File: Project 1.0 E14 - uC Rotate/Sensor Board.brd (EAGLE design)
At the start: 40 x 75 mm, 97 parts, among them IC1 LT1963EST-1.5, IC2 LT1963EST-1.5, IC4 LT1963EST-1.5

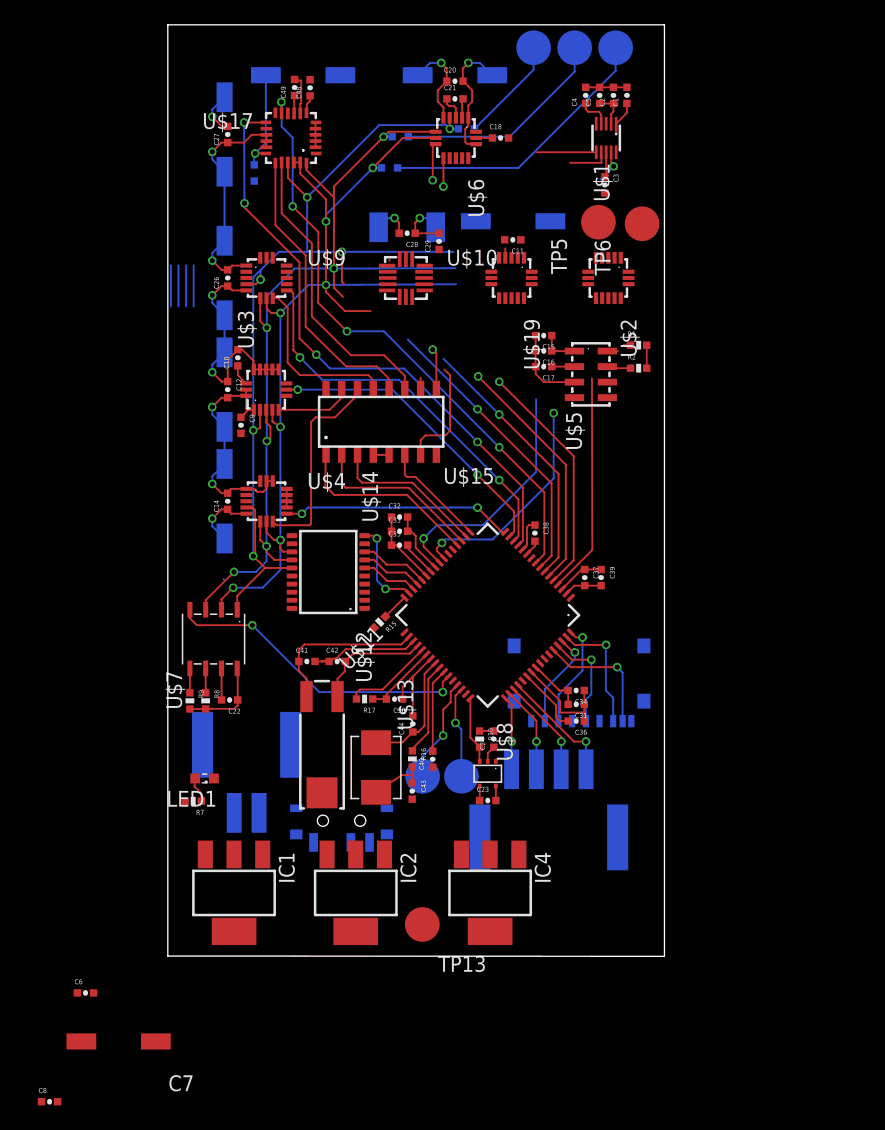
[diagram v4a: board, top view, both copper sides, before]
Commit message: Sensor Board: Chnaged 3:8 mux for a 4:10 mux and removed traces that were no longer valid, rerouting is now needed
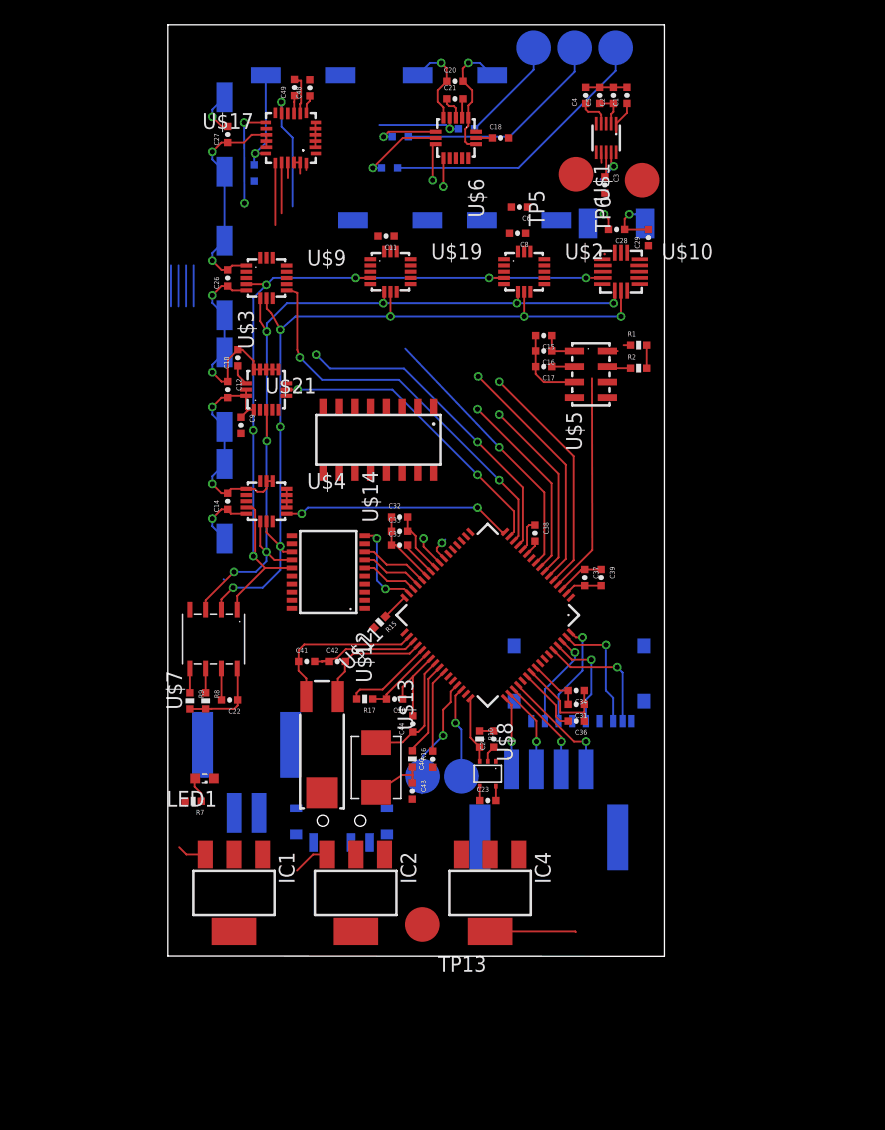
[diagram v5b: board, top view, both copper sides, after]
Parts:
- removed U$15: CD74HC138, Kas-Buffers & Level Shifters:SOIC-16
- added U$21: SN74HC42, Kas-Buffers & Level Shifters:SOIC-16
- moved C8 79.5 mm to (28.2, 58.2), turned to 180 degrees
- moved C7 73.6 mm to (28.3, 59.3), flipped to the bottom
- moved C6 72.3 mm to (28.3, 60.3), turned to 180 degrees
- moved U$10 17.3 mm to (36.5, 55.1)
- moved C29 16.9 mm to (38.7, 57.9)
- moved C19 16.9 mm to (36.1, 59.0)
- moved C28 16.9 mm to (36.1, 58.5)
- moved C11 10.2 mm to (17.6, 58.0)
- moved C54 9.91 mm to (17.9, 59.3)
- moved U$19 9.77 mm to (17.9, 55.1), turned to 0 degrees
- moved U$2 6.80 mm to (28.7, 55.1), turned to 0 degrees
- moved TP5 4.26 mm to (32.9, 63.0)
- moved TP6 3.51 mm to (38.2, 62.5)
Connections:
- removed net CS-ENABLE: U$11.P$17, U$15.P$6
- new net INT2-H3LIS331: U$11.P$10, U$2.P$9
- new net SPI-ADDR3: U$11.P$20, U$21.P$12
- net 3.3V: now also U$21.P$16; no longer U$15.P$16
- net CS-ADT7310: now also U$21.P$1; no longer U$11.P$43
- net CS-ADXL362: now also U$21.P$4; no longer U$15.P$10
- net CS-H3LIS331DLTR: no longer U$11.P$10
- net CS-LIS3DH: now also U$21.P$11; no longer U$15.P$13
- net CS-LPS331: now also U$21.P$10; no longer U$15.P$14
- net CS-LSGD: now also U$21.P$9; no longer U$15.P$15
- net CS-LSM303: now also U$21.P$3; no longer U$15.P$9
- net CS-LSM9D30-G: now also U$21.P$6; no longer U$15.P$12
- net CS-LSM9DS0-XM: now also U$21.P$5; no longer U$15.P$11
- net CS-MAX21000: now also U$21.P$2; no longer U$15.P$7
- net GND: now also U$21.P$8; no longer U$15.P$4, U$15.P$5, U$15.P$8
- net SPI-ADDR0: now also U$11.P$17, U$21.P$15; no longer U$11.P$20, U$15.P$1
- net SPI-ADDR1: now also U$11.P$18, U$21.P$14; no longer U$11.P$19, U$15.P$2
- net SPI-ADDR2: now also U$11.P$19, U$21.P$13; no longer U$11.P$18, U$15.P$3
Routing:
- net CS-ADT7310: track 25.0 -> 0.00 mm, vias 2 -> 0
- net SDA-0: track 26.3 -> 4.37 mm
- net CS-LSM9DS0-XM: track 23.9 -> 4.09 mm
- net SCL-0: track 22.9 -> 4.29 mm, vias 2 -> 1
- net CS-LSM9D30-G: track 23.5 -> 5.06 mm
- net LSM9D-INT-G: track 48.8 -> 31.8 mm, vias 4 -> 2
- net CS-LPS331: track 16.6 -> 0.00 mm
- net SPI-ADDR0: track 15.4 -> 0.00 mm
- net LSM9D-INT1-XM: track 48.7 -> 34.5 mm
- net CS-LIS3DH: track 14.2 -> 0.00 mm
- net SPI-ADDR1: track 13.9 -> 0.00 mm
- net SPI-ADDR2: track 12.5 -> 0.00 mm
- net CS-MAX21000: track 9.00 -> 0.00 mm
- net CS-ENABLE: track 8.79 -> 0.00 mm
- net SCLK-B: track 82.9 -> 74.8 mm, vias 6 -> 7
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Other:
- board text removed: "Change for 16:1 Mux"

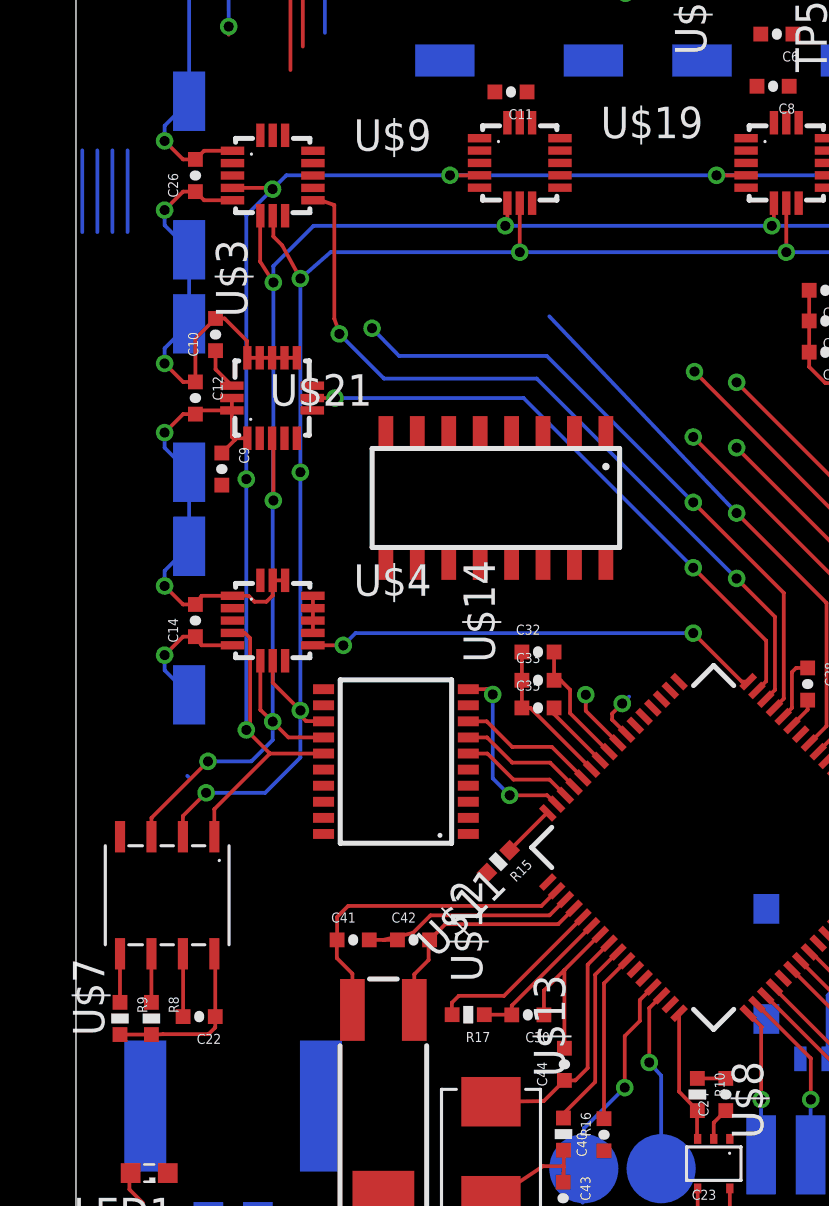
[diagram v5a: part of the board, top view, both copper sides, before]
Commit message: Sensor Test Board: Changed tmperature sensor for ADT7301 using a smaller package (SOT32-6). Reconnected CS traces in a organised fasion. Hid Power and GND traces.
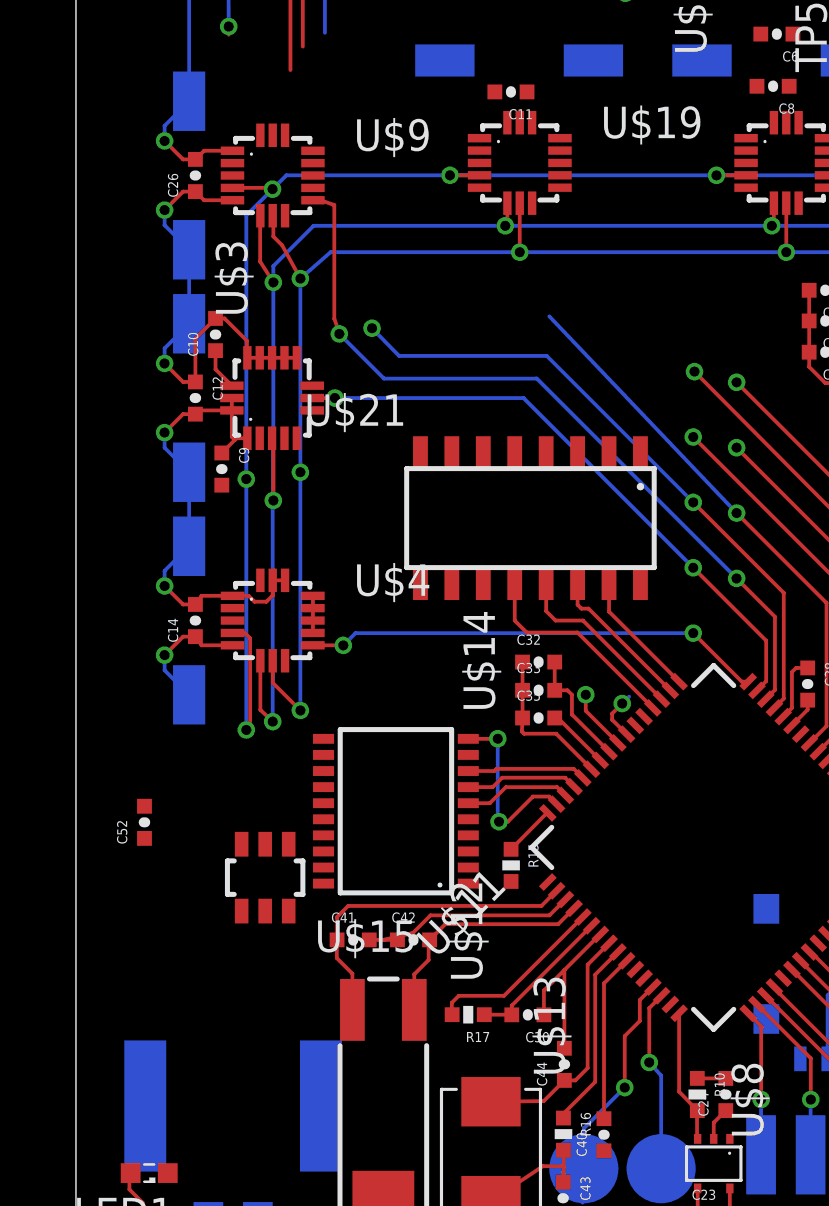
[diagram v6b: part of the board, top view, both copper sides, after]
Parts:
- removed C22: 0.1uF, Kas-Passives:0402-CAP
- removed R8, R9: 10k, Kas-Passives:0402-RES
- removed U$7: ADT7310, Kas-Sensors:SOIC-8(5X6.2)
- added C52: 0.1uF, Kas-Passives:0402-CAP
- added U$15: ADT7301, Kas-Sensors:SOT23-6
- moved U$14 2.01 mm to (12.9, 28.9)
- moved U$21 1.62 mm to (18.4, 40.8)
- moved R15 0.54 mm to (17.6, 26.7), turned to 270 degrees
- moved C35 0.41 mm to (18.7, 32.7)
- moved C32 0.41 mm to (18.7, 35.0)
- moved C33 0.41 mm to (18.7, 33.8)
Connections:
- net CS-LSGD renamed CS-LS3GD20
- removed net CS-ADT7310: U$21.P$1, U$7.P$4
- removed net CT-ADT7310: R8.1, U$7.P$6
- removed net INT-ADT7310: R9.1, U$7.P$5
- new net CS-ADT7301: U$15.P$5, U$21.P$11
- new net N$2: C52.1, U$15.P$3
- net 3.3V: no longer C22.1, R8.2, R9.2, U$7.P$8
- net CS-ADXL362: now also U$21.P$1; no longer U$21.P$4
- net CS-H3LIS331DLTR: now also U$21.P$2
- net CS-LIS3DH: now also U$21.P$7; no longer U$21.P$11
- net CS-MAX21000: now also U$21.P$4; no longer U$21.P$2
- net GND: now also C52.2, U$15.P$1; no longer C22.2, U$7.P$7
- net MISO-B: now also U$15.P$6; no longer U$7.P$2
- net MOSI-B: now also U$15.P$2; no longer U$7.P$3
- net SCLK-B: now also U$15.P$4; no longer U$7.P$1
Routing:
- net N$29: track 16.5 -> 0.00 mm
- net MOSI-B: track 73.7 -> 63.7 mm, vias 8 -> 7
- net MISO-B: track 74.5 -> 65.0 mm, vias 8 -> 7
- net SPI-ADDR3: track 0.00 -> 8.51 mm
- net SCLK-B: track 74.8 -> 67.0 mm
- net 3.3V: track 97.8 -> 90.5 mm
- net SPI-ADDR2: track 0.00 -> 7.22 mm
- net SPI-ADDR1: track 0.00 -> 6.01 mm
- net SPI-ADDR0: track 0.00 -> 5.11 mm
- net N$28: track 3.30 -> 0.00 mm
- net N$26: track 3.30 -> 0.00 mm
- net GND: track 91.7 -> 89.3 mm
- net INT-ADT7310: track 1.96 -> 0.00 mm
- net CT-ADT7310: track 1.96 -> 0.00 mm
- net MISO-A: track 5.57 -> 4.81 mm
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
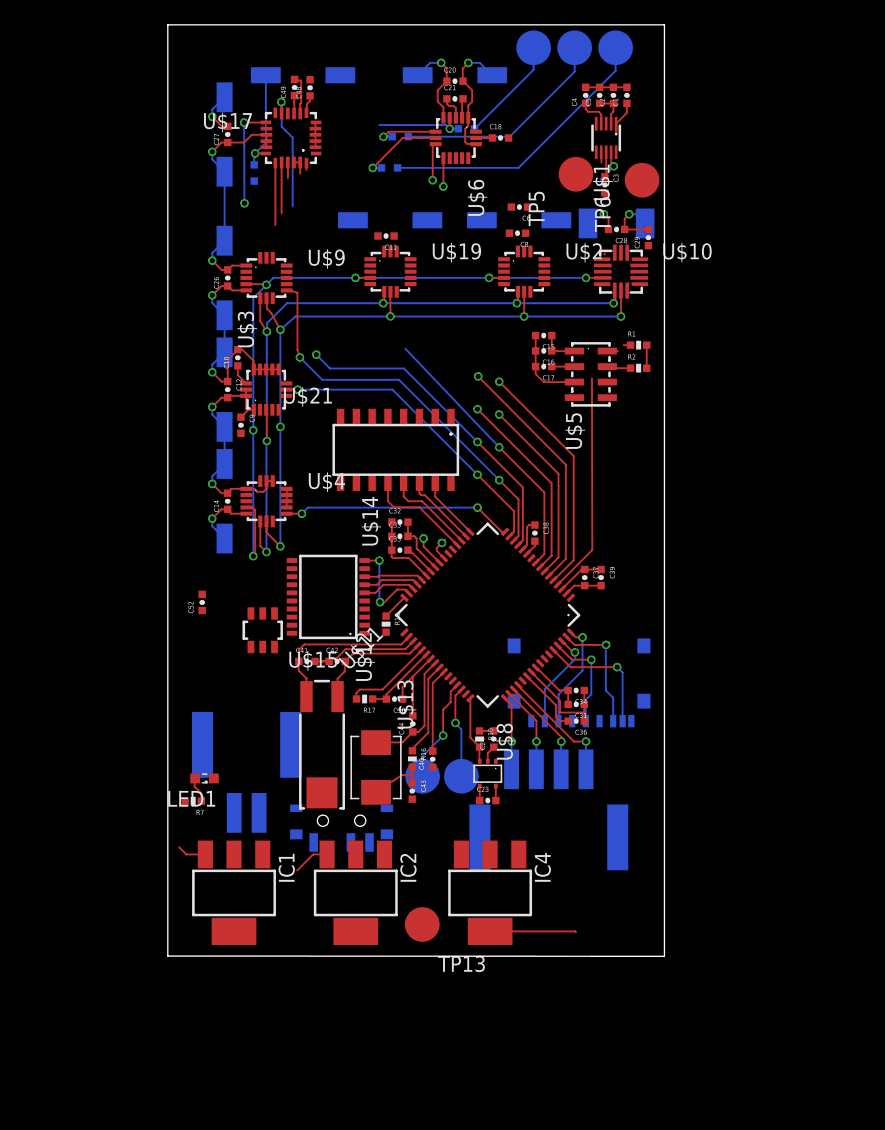
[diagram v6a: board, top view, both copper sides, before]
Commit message: Sensor Test Board: Swapped order of magnotometers, reorganised CS traces to prevent overlaps and connected new teperature sensor. Removed LS9D Vio bulk and decoupling capacitors. SPI test points were disconected but not removed. SPI vertical traces were spaced correctly with a minimum of 6x trace with spacing between traces.
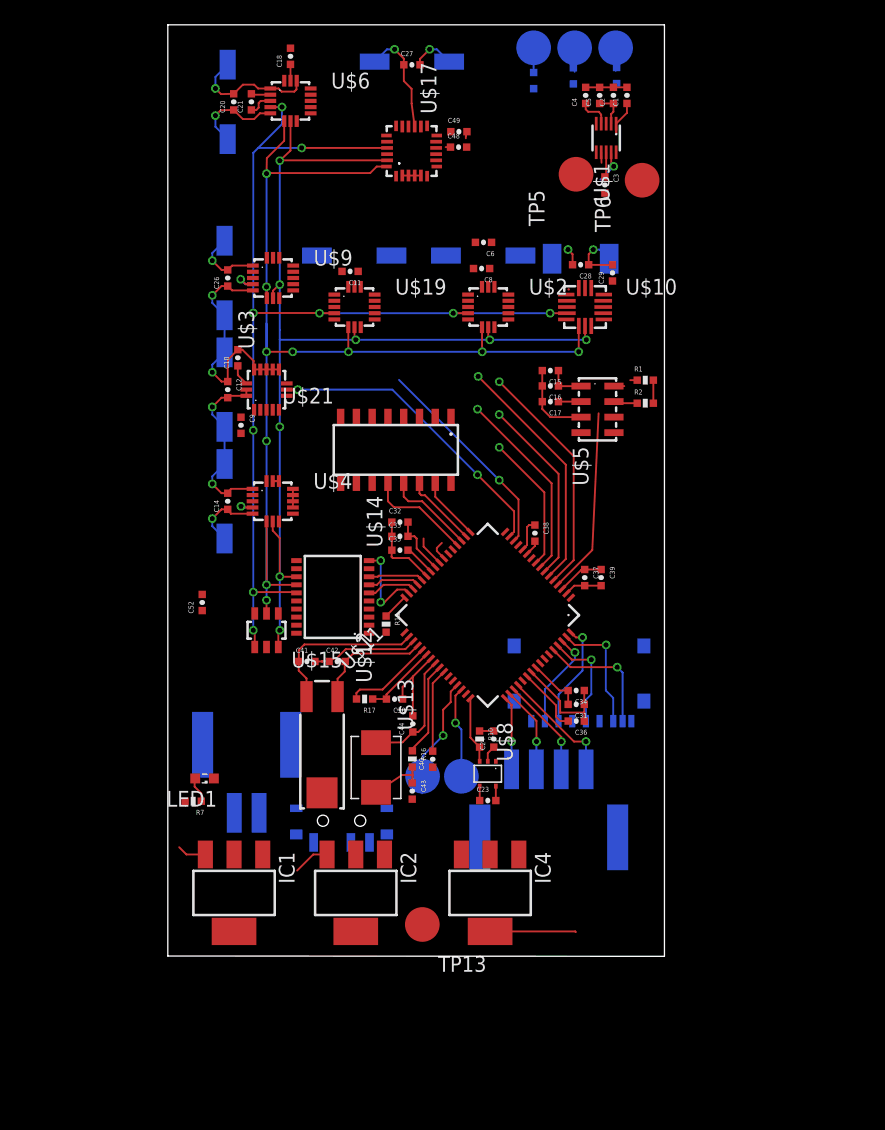
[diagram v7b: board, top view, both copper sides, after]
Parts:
- removed C50: 10uF, Kas-Passives:4.3X7.3SMD
- removed C51: 100nF, Kas-Passives:0402-CAP
- moved R6 19.7 mm to (36.1, 70.9), turned to 90 degrees
- moved C46 18.4 mm to (4.83, 68.8), turned to 270 degrees
- moved C18 18.2 mm to (9.88, 72.5), turned to 90 degrees
- moved C20 17.9 mm to (5.31, 68.8), turned to 90 degrees
- moved C21 16.4 mm to (6.73, 68.8), turned to 90 degrees
- moved C25 16.2 mm to (19.7, 72.0), turned to 180 degrees
- moved C27 15.9 mm to (19.7, 71.8), turned to 0 degrees
- moved R4 14.8 mm to (32.7, 70.9), turned to 90 degrees
- moved C49 13.7 mm to (23.4, 66.4), turned to 0 degrees
- moved U$6 13.7 mm to (9.88, 68.9), turned to 0 degrees
- moved C48 12.9 mm to (23.4, 65.2), turned to 0 degrees
- moved U$17 9.77 mm to (19.6, 64.8), turned to 90 degrees
- moved R3 6.66 mm to (29.5, 70.5), turned to 90 degrees
- moved C29 4.06 mm to (35.8, 55.0)
- moved C6 4.06 mm to (25.4, 57.5)
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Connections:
- net 3.0V: no longer C50.P$1, C51.1
- net CS-LSM303: now also U$21.P$6; no longer U$21.P$3
- net CS-LSM9D30-G: now also U$21.P$4; no longer U$21.P$6
- net CS-LSM9DS0-XM: now also U$21.P$3; no longer U$21.P$5
- net CS-MAX21000: now also U$21.P$5; no longer U$21.P$4
- net GND: no longer C50.P$2, C51.2
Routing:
- net LSM9D-INT1-XM: track 34.5 -> 0.00 mm, vias 4 -> 0
- net MOSI-B: track 63.7 -> 92.0 mm, vias 7 -> 10
- net SCLK-B: track 67.0 -> 91.3 mm, vias 7 -> 11
- net MISO-B: track 65.0 -> 86.7 mm, vias 7 -> 8
- net N$34: track 22.7 -> 1.85 mm
- net LSM9D-INT-G: track 31.8 -> 11.1 mm, vias 2 -> 1
- net INT2-LPS331: track 18.6 -> 0.00 mm, vias 2 -> 0
- net N$33: track 17.5 -> 1.93 mm
- net INT2-LIS3DH: track 32.0 -> 17.3 mm, vias 2 -> 1
- net 3.0V: track 10.8 -> 2.35 mm, vias 1 -> 0
- net 3.3V: track 90.5 -> 82.6 mm
- net N$32: track 8.50 -> 1.77 mm
- net CS-LSM9D30-G: track 5.06 -> 0.00 mm
- net CS-LSM9DS0-XM: track 4.09 -> 0.00 mm
- net CS-LSM303: track 3.39 -> 0.48 mm, vias 1 -> 0
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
